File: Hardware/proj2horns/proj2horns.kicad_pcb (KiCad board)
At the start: 2 copper layers, 32.5 x 30.5 mm, 17 parts, among them J1 Conn_01x03, J2 Conn_01x02, J3 Conn_01x02, J4 Conn_01x02, Q1 Q_NMOS

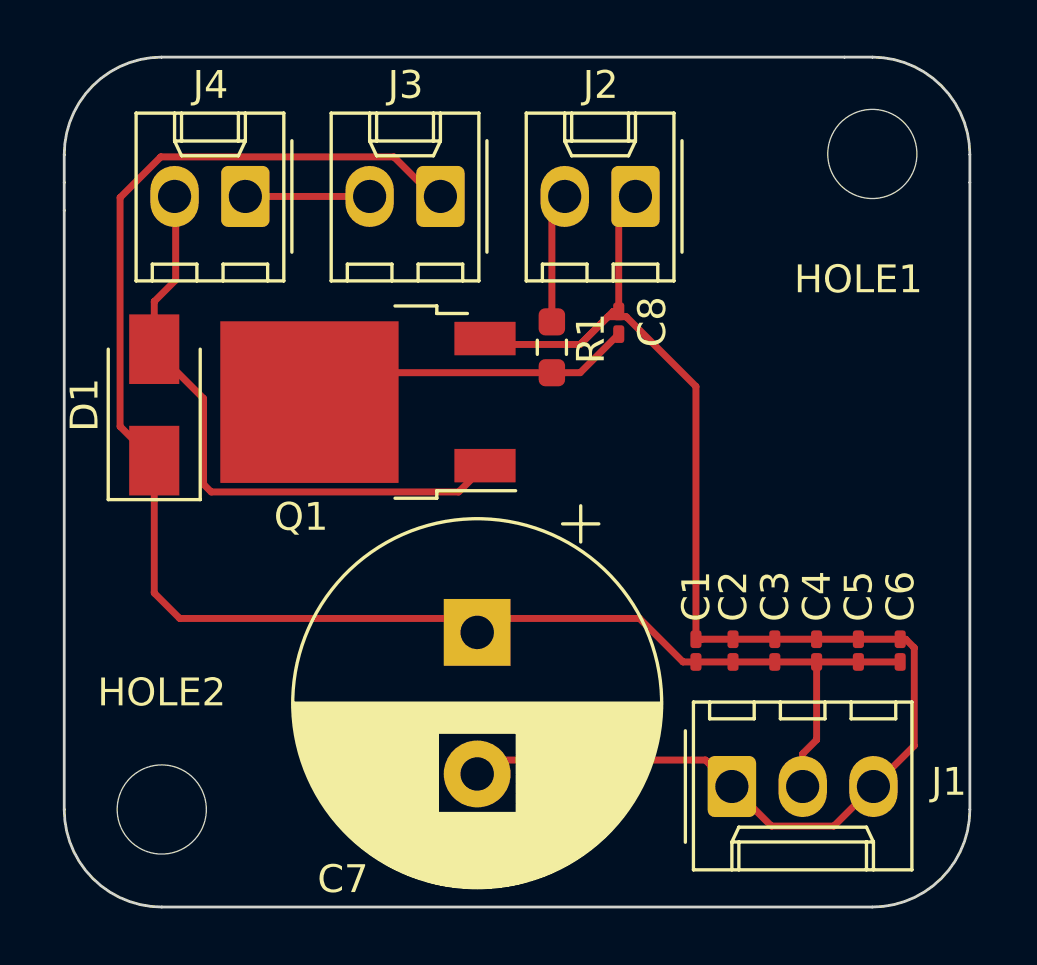
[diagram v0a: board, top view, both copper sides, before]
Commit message: adjusted mounting hole distance from PCB edge for gbr/drl check
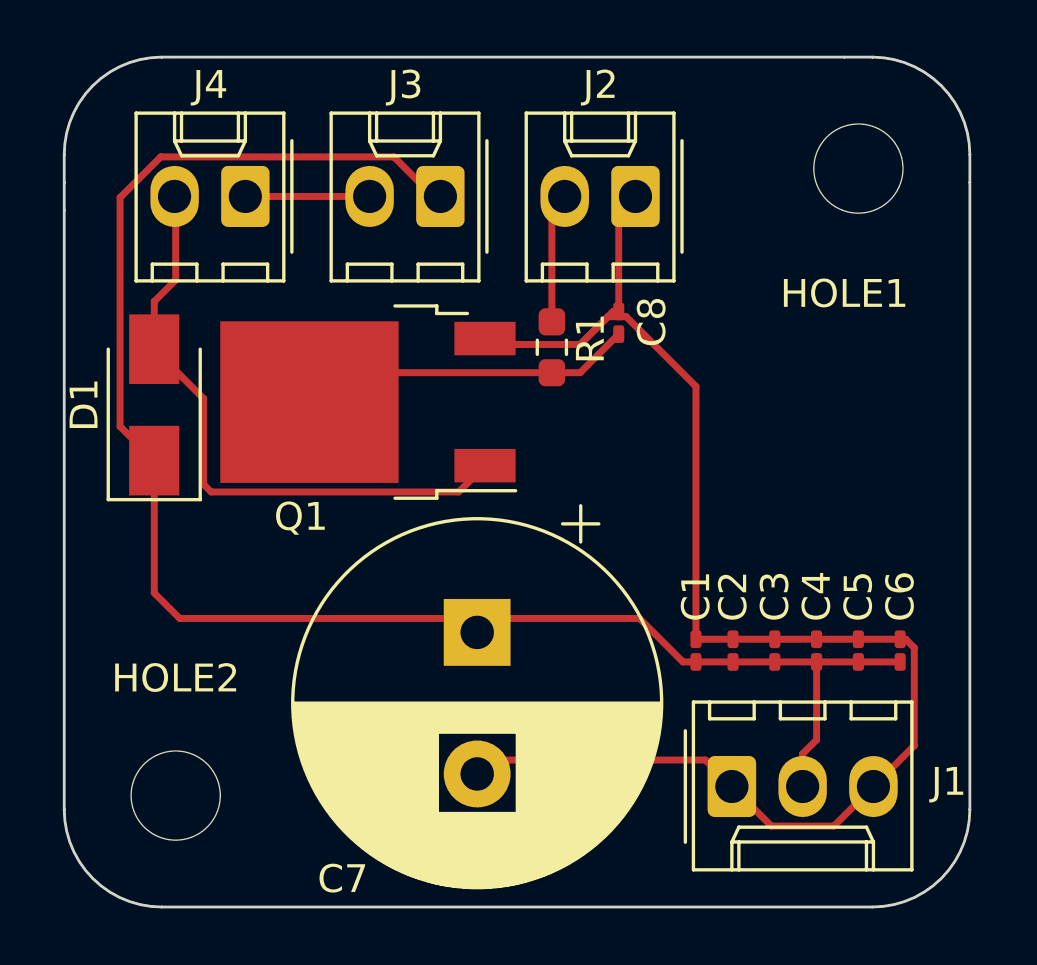
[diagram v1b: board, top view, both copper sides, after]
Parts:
- moved HOLE1 0.73 mm to (200.0, 103.5)
- moved HOLE2 0.71 mm to (175.5, 126.0)
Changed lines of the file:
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@@
 	(footprint "MountingHole:MountingHole_3.2mm_M3"
 		(layer "F.Cu")
-		(at 200.5 102.974874)
+		(at 200 103.5)
 		(descr "Mounting Hole 3.2mm, no annular, M3")
 		(tags "mounting hole 3.2mm no annular m3")
@@
 	(footprint "MountingHole:MountingHole_3.2mm_M3"
 		(layer "F.Cu")
-		(at 175 126.5)
+		(at 175.5 126)
 		(descr "Mounting Hole 3.2mm, no annular, M3")
 		(tags "mounting hole 3.2mm no annular m3")

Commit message: fixed copper zones: 24V to F.Cu, GND to B.Cu
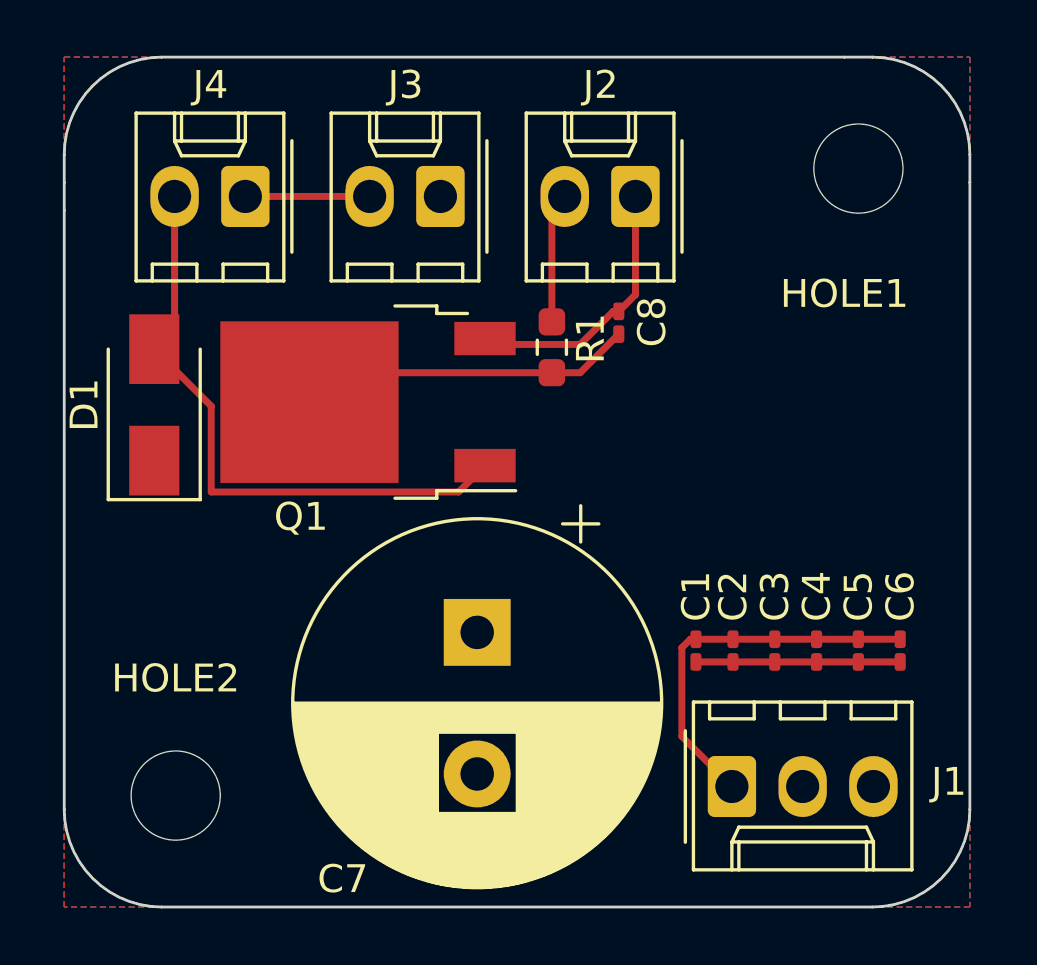
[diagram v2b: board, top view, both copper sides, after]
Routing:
- net +24V: track 60.3 -> 7.33 mm
- net GND: track 55.2 -> 23.4 mm
- net /HORN_IN: track 23.4 -> 22.0 mm
- added copper zone on F.Cu, net +24V
- added copper zone on B.Cu, net GND
